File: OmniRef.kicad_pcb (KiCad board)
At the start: 2 copper layers, 79.7 x 50.7 mm, 62 parts, among them J1 4mm Banana Jack Pair, J2 4mm Banana Jack Pair, Q1 PMBT3906, SW1 SW_SPDT, U1 REFERENCE IC, U2 LP2951, U3 REFERENCE IC

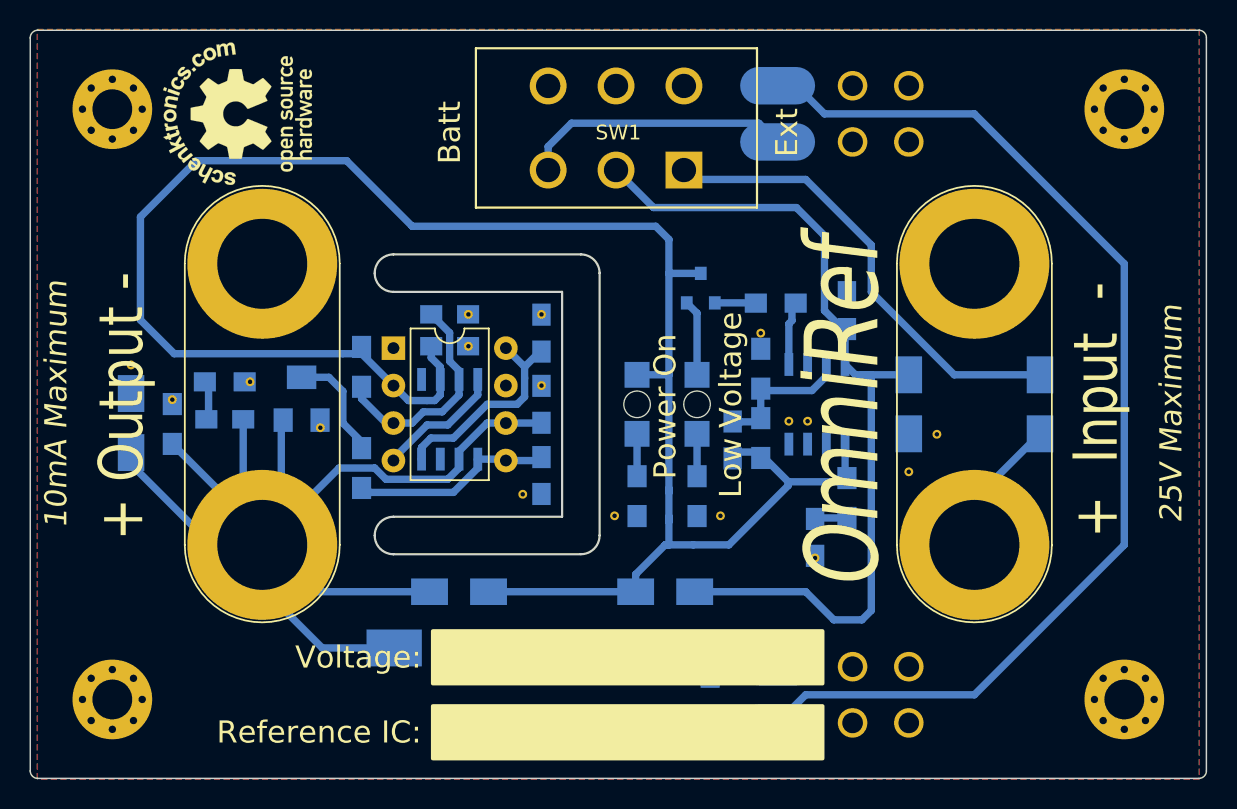
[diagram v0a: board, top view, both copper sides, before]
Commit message: Renamed to OmniRef.  Made some final changes to schematic and board before generating gerbers.
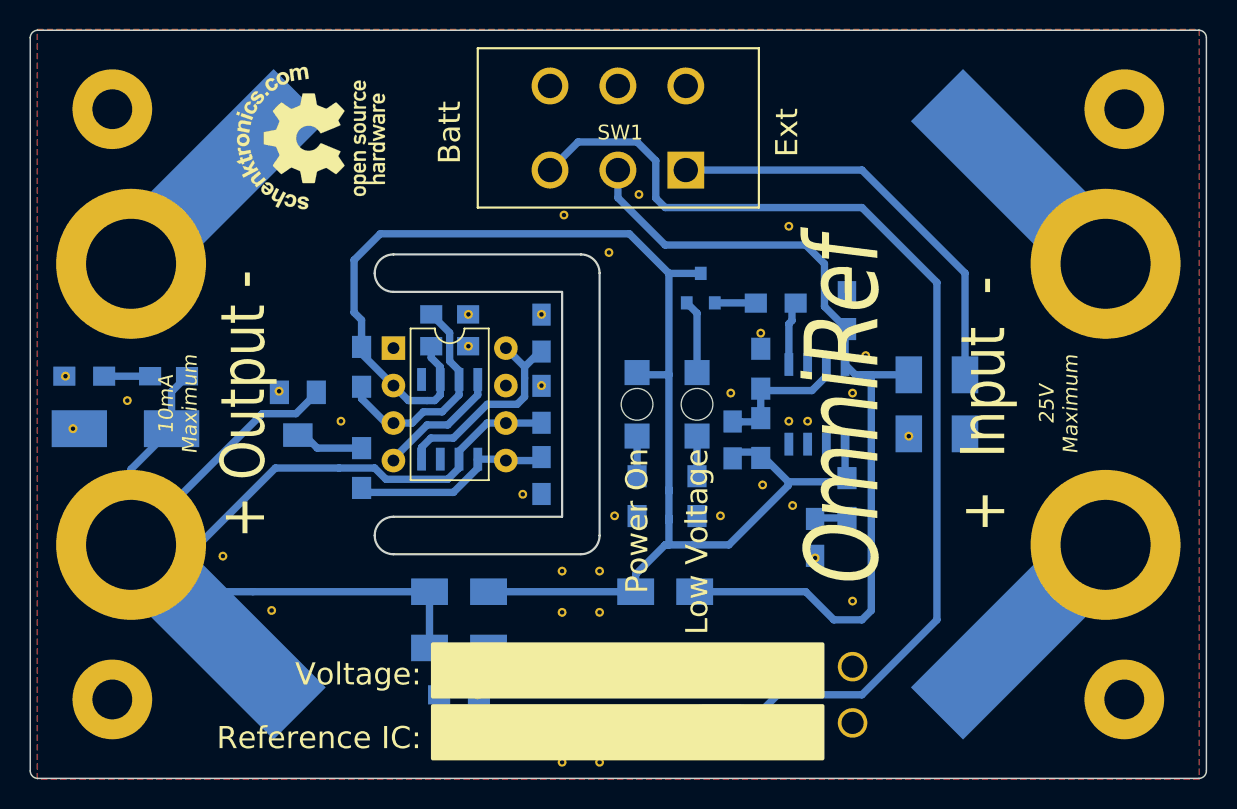
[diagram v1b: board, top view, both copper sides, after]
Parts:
- removed BT2: Battery, _NTSFootprints:9vClipWireLeads
- removed R11: 0, Resistors_SMD:R_0805_HandSoldering
- added REF**: 1pin, _NTSFootprints:Via_Tented_0.3mm, F.Cu at (151.8, 82.4)
- added REF**: 1pin, _NTSFootprints:Via_Tented_0.3mm, F.Cu at (120.7, 97.2)
- added REF**: 1pin, _NTSFootprints:Via_Tented_0.3mm, F.Cu at (117.3, 93.5)
- added REF**: 1pin, _NTSFootprints:Via_Tented_0.3mm, F.Cu at (110.9, 82.9)
- added REF**: 1pin, _NTSFootprints:Via_Tented_0.3mm, F.Cu at (125.3, 84.3)
- added REF**: 1pin, _NTSFootprints:Via_Tented_0.3mm, F.Cu at (140.5, 70.4)
- added REF**: 1pin, _NTSFootprints:Via_Tented_0.3mm, F.Cu at (143.5, 72.9)
- added REF**: 1pin, _NTSFootprints:Via_Tented_0.3mm, F.Cu at (140.3, 94.5)
- added REF**: 1pin, _NTSFootprints:Via_Tented_0.3mm, F.Cu at (160.0, 82.4)
- added REF**: 1pin, _NTSFootprints:Via_Tented_0.3mm, F.Cu at (160.9, 79.9)
- added REF**: 1pin, _NTSFootprints:Via_Tented_0.3mm, F.Cu at (145.5, 69.0)
- added REF**: 1pin, _NTSFootprints:Via_Tented_0.3mm, F.Cu at (155.7, 71.1)
- added REF**: 1pin, _NTSFootprints:Via_Tented_0.3mm, F.Cu at (160.0, 96.5)
- added REF**: 1pin, _NTSFootprints:Via_Tented_0.3mm, F.Cu at (156.0, 90.0)
- added REF**: 1pin, _NTSFootprints:Via_Tented_0.3mm, F.Cu at (153.9, 88.6)
- added REF**: 1pin, _NTSFootprints:Via_Tented_0.3mm, F.Cu at (140.3, 97.3)
- added REF**: 1pin, _NTSFootprints:Via_Tented_0.3mm, F.Cu at (142.9, 97.3)
- added REF**: 1pin, _NTSFootprints:Via_Tented_0.3mm, F.Cu at (142.9, 107.4)
- added REF**: 1pin, _NTSFootprints:Via_Tented_0.3mm, F.Cu at (140.3, 107.4)
- D5, D7: footprint _NTSFootprints:LED_1206_1.7mmHole -> _NTSFootprints:LED_1206_2.15mmHole
- J1: footprint _NTSFootprints:Banana_Jack_2pin_.25_.75 -> _NTSFootprints:Banana_Jack_2pin_Wings_45M_.25_.75
- J2: footprint _NTSFootprints:Banana_Jack_2pin_.25_.75 -> _NTSFootprints:Banana_Jack_2pin_Wings_.25_.75
- REF** (x4): footprint Mounting_Holes:MountingHole_2.7mm_M2.5_Pad_Via -> Mounting_Holes:MountingHole_2.7mm_M2.5_Pad
- moved BT1 39.6 mm to (151.1, 104.8)
- moved REF** 30.8 mm to (135.3, 99.7)
- moved D6 26.9 mm to (133.3, 99.7), turned to 0 degrees
- moved R8 26.7 mm to (133.3, 102.9), turned to 0 degrees
- moved REF** 26.2 mm to (134.6, 102.9)
- moved C9 26.0 mm to (110.7, 84.8), turned to 180 degrees
- moved REF** 22.3 mm to (121.2, 82.3)
- moved REF** 22.0 mm to (142.9, 94.5)
- moved REF** 16.8 mm to (107.2, 84.8)
- moved R6 9.53 mm to (108.0, 81.3), turned to 180 degrees
- moved J2 8.89 mm to (111.1, 92.7)
- moved J1 8.89 mm to (177.2, 92.7)
- moved REF** 7.41 mm to (106.7, 81.3)
- moved G*** 5.22 mm to (123.1, 65.2)
- moved D1 5.08 mm to (167.6, 83.2)
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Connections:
- BT1 pad 0: (no net) -> GND
- BT1 pad 2: Net-(BT1-Pad2) -> GND
- SW1 pad 4: (no net) -> GND
- SW1 pad 5: (no net) -> GND
- SW1 pad 6: (no net) -> GND
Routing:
- net Net-(BT1-Pad2): track 80.9 -> 0.00 mm
- net BAT+: track 18.3 -> 72.8 mm
- net V+: track 134.4 -> 99.1 mm
- net Net-(D1-Pad2): track 11.8 -> 0.00 mm
- net Net-(R2-Pad1): track 7.82 -> 5.36 mm
- net Net-(C7-Pad1): track 94.1 -> 91.8 mm
- net Net-(D1-Pad1): track 31.9 -> 29.6 mm
- net Net-(C7-Pad2): track 2.60 -> 3.12 mm

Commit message: Generated Gerbers.  Fixed a couple unconnected pads the DRC found.
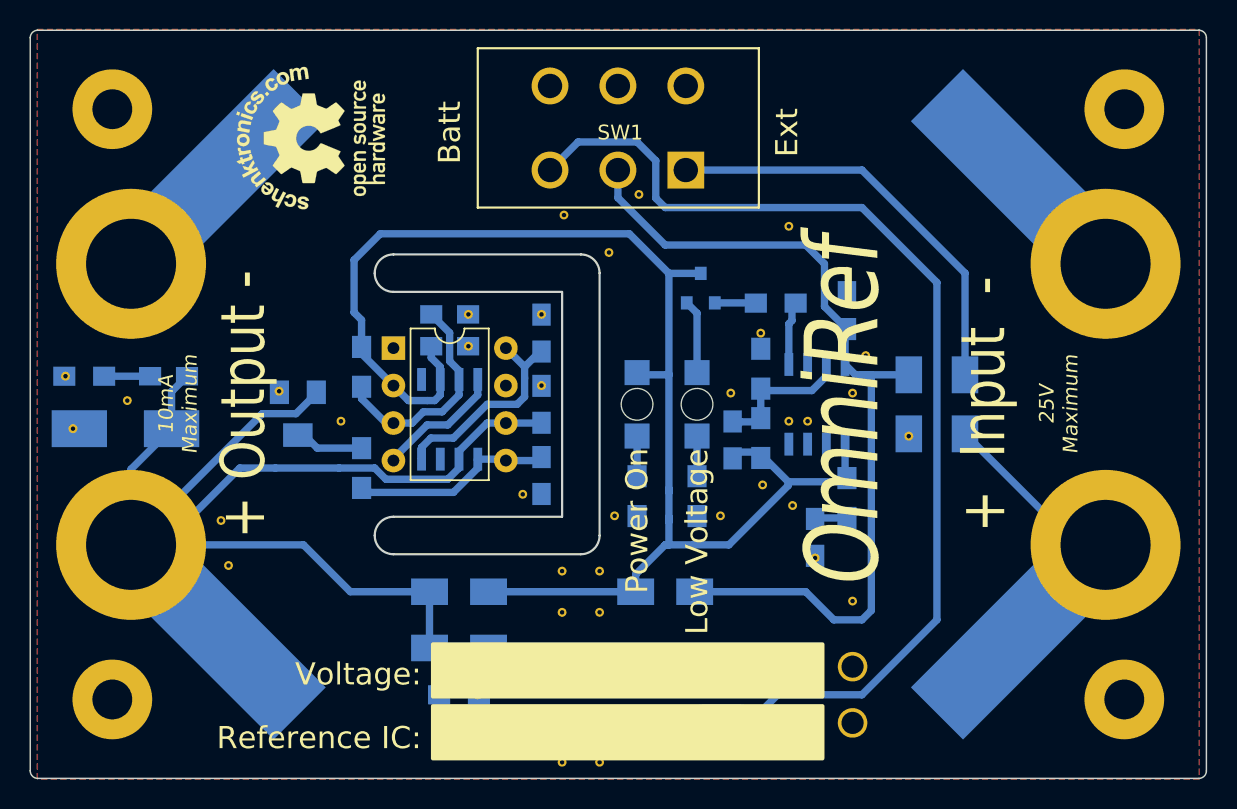
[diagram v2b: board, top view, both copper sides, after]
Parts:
- moved REF** 4.22 mm to (117.7, 94.1)
- moved REF** 2.42 mm to (117.2, 91.1)
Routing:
- net Net-(D1-Pad2): track 0.00 -> 21.8 mm
- net Net-(C7-Pad1): track 91.8 -> 103.4 mm
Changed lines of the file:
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@@
   (general
     (links 121)
-    (no_connects 2)
-    (area 104.242399 57.785799 184.047601 108.584201)
+    (no_connects 0)
+    (area 96.297857 45.619999 191.992143 113.47)
     (thickness 1.6)
     (drawings 38)
-    (tracks 172)
+    (tracks 178)
     (zones 0)
     (modules 79)
@@
     (33 F.Adhes user hide)
     (34 B.Paste user hide)
-    (35 F.Paste user hide)
-    (36 B.SilkS user)
+    (35 F.Paste user)
+    (36 B.SilkS user hide)
     (37 F.SilkS user hide)
     (38 B.Mask user hide)
     (39 F.Mask user hide)
     (40 Dwgs.User user hide)
-    (41 Cmts.User user hide)
+    (41 Cmts.User user)
     (42 Eco1.User user hide)
     (43 Eco2.User user hide)
@@
     (visible_elements 7FFED669)
     (pcbplotparams
-      (layerselection 0x00030_80000001)
+      (layerselection 0x012f0_80000001)
       (usegerberextensions false)
       (excludeedgelayer true)
@@
       (outputformat 1)
       (mirror false)
-      (drillshape 1)
+      (drillshape 0)
       (scaleselection 1)
-      (outputdirectory ""))
+      (outputdirectory Gerbers/))
   )
   (net 0 "")
@@
   )
   (module _NTSFootprints:Via_Tented_0.3mm (layer F.Cu)
-    (at 120.65 97.155)
+    (at 117.729 94.107)
     (descr "module 1 pin (ou trou mecanique de percage)")
     (tags DEV)
@@
   )
   (module _NTSFootprints:Via_Tented_0.3mm (layer F.Cu)
-    (at 117.348 93.472)
+    (at 117.221 91.059)
     (descr "module 1 pin (ou trou mecanique de percage)")
     (tags DEV)
@@
   (segment (start 159.639 90.885) (end 157.547 90.885) (width 0.5) (layer B.Cu) (net 5))
   (segment (start 157.547 90.885) (end 157.48 90.952) (width 0.5) (layer B.Cu) (net 5))
+  (segment (start 131.35 95.885) (end 125.984 95.885) (width 0.5) (layer B.Cu) (net 6))
+  (segment (start 122.809 92.71) (end 111.125 92.71) (width 0.5) (layer B.Cu) (net 6))
+  (segment (start 125.984 95.885) (end 122.809 92.71) (width 0.5) (layer B.Cu) (net 6))
+  (segment (start 120.904 87.503) (end 118.491 87.503) (width 0.5) (layer B.Cu) (net 6))
+  (segment (start 132.588 88.265) (end 128.397 88.265) (width 0.5) (layer B.Cu) (net 6))
+  (segment (start 128.397 88.265) (end 127.635 87.503) (width 0.5) (layer B.Cu) (net 6))
+  (segment (start 127.635 87.503) (end 125.222 87.503) (width 0.5) (layer B.Cu) (net 6))
+  (segment (start 133.35 87.503) (end 132.588 88.265) (width 0.5) (layer B.Cu) (net 6))
+  (segment (start 120.904 87.503) (end 125.222 87.503) (width 0.5) (layer B.Cu) (net 6))
+  (segment (start 118.491 87.503) (end 113.284 92.71) (width 0.5) (layer B.Cu) (net 6))
+  (segment (start 113.284 92.71) (end 111.125 92.71) (width 0.5) (layer B.Cu) (net 6))
   (segment (start 132 102.87) (end 132 100.345) (width 0.5) (layer B.Cu) (net 6))
   (segment (start 132 100.345) (end 131.35 99.695) (width 0.5) (layer B.Cu) (net 6))
@@
   (segment (start 111.125 87.58) (end 113.869 84.836) (width 0.5) (layer B.Cu) (net 6))
   (segment (start 131.35 99.695) (end 131.35 95.885) (width 0.5) (layer B.Cu) (net 6))
-  (segment (start 131.35 95.885) (end 119.38 95.885) (width 0.5) (layer B.Cu) (net 6))
-  (segment (start 119.38 95.885) (end 116.84 95.885) (width 0.5) (layer B.Cu) (net 6))
   (segment (start 116.84 95.885) (end 113.665 92.71) (width 0.5) (layer B.Cu) (net 6))
   (segment (start 113.665 92.71) (end 111.125 92.71) (width 0.5) (layer B.Cu) (net 6))
   (segment (start 123.678 82.37) (end 123.678 82.443) (width 0.5) (layer B.Cu) (net 6))
   (segment (start 123.678 82.443) (end 122.301 83.82) (width 0.5) (layer B.Cu) (net 6))
-  (segment (start 122.301 83.82) (end 120.015 83.82) (width 0.5) (layer B.Cu) (net 6))
   (segment (start 120.015 83.82) (end 111.125 92.71) (width 0.5) (layer B.Cu) (net 6))
+  (segment (start 122.301 83.82) (end 120.015 83.82) (width 0.5) (layer B.Cu) (net 6))
   (segment (start 111.125 92.71) (end 115.697 92.71) (width 0.5) (layer B.Cu) (net 6))
-  (segment (start 115.697 92.71) (end 120.904 87.503) (width 0.5) (layer B.Cu) (net 6))
-  (segment (start 120.904 87.503) (end 125.222 87.503) (width 0.5) (layer B.Cu) (net 6))
   (segment (start 136.591 84.521) (end 136.525 84.455) (width 0.5) (layer B.Cu) (net 6))
   (segment (start 135.255 84.455) (end 136.525 84.455) (width 0.5) (layer B.Cu) (net 6))
   (segment (start 133.35 86.901) (end 133.35 87.503) (width 0.5) (layer B.Cu) (net 6))
-  (segment (start 133.35 87.503) (end 132.588 88.265) (width 0.5) (layer B.Cu) (net 6))
-  (segment (start 127.635 87.503) (end 125.222 87.503) (width 0.5) (layer B.Cu) (net 6))
-  (segment (start 128.397 88.265) (end 127.635 87.503) (width 0.5) (layer B.Cu) (net 6))
-  (segment (start 132.588 88.265) (end 128.397 88.265) (width 0.5) (layer B.Cu) (net 6))
   (segment (start 136.525 84.455) (end 138.918 84.455) (width 0.5) (layer B.Cu) (net 6))
   (segment (start 138.918 84.455) (end 138.938 84.435) (width 0.5) (layer B.Cu) (net 6))
@@
   (segment (start 136.525 84.455) (end 136.017 84.455) (width 0.5) (layer F.Cu) (net 6))
   (segment (start 109.3 81.28) (end 112.415 81.28) (width 0.5) (layer B.Cu) (net 7))
+  (segment (start 170.688 99.187) (end 177.165 92.71) (width 0.5) (layer B.Cu) (net 8))
+  (segment (start 177.165 92.71) (end 175.165 92.71) (width 0.5) (layer B.Cu) (net 8))
+  (segment (start 175.165 92.71) (end 167.64 85.185) (width 0.5) (layer B.Cu) (net 8))
   (segment (start 149.479 87.673) (end 149.479 85.185) (width 0.5) (layer B.Cu) (net 9))
   (segment (start 149.749 85.296) (end 149.86 85.185) (width 0.5) (layer B.Cu) (net 9))
